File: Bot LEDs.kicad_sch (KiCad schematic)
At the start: 28 parts

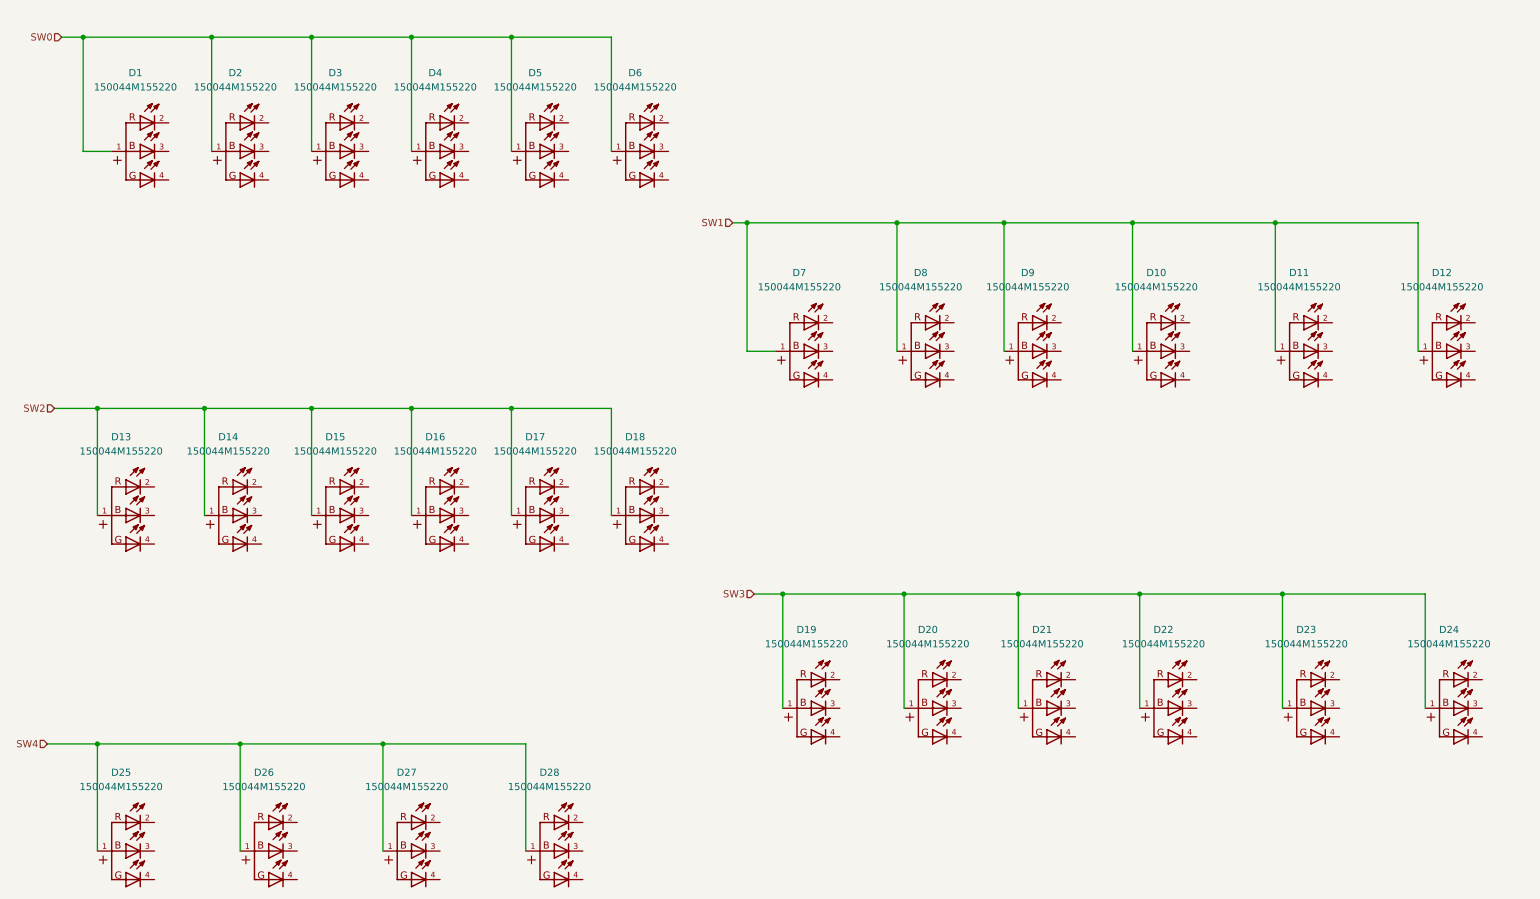
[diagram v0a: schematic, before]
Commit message: Initial complete implementation of LEDS.
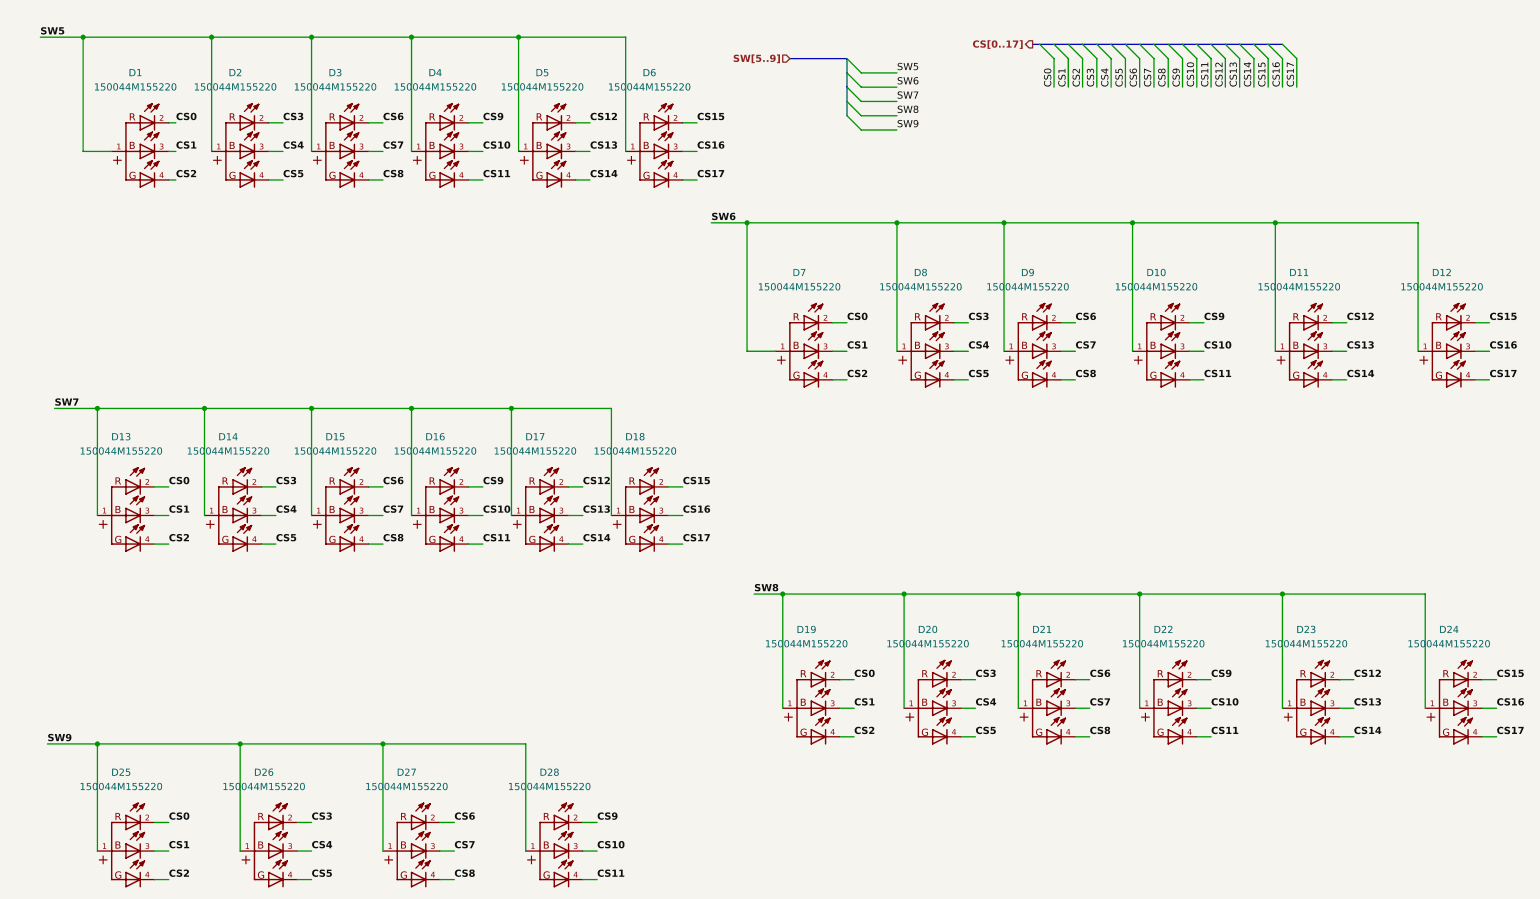
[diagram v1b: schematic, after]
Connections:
- net CS9: now reaches D28.2
- net CS9: now also D10.2, D16.2, D22.2, D4.2
- net CS10: now reaches D28.3
- net CS10: now also D10.3, D16.3, D22.3, D4.3
- net CS11: now reaches D28.4
- net CS11: now also D10.4, D16.4, D22.4, D4.4
- net CS12: now reaches D23.2
- net CS12: now also D11.2, D17.2, D5.2
- net CS13: now reaches D23.3
- net CS13: now also D11.3, D17.3, D5.3
- net CS14: now reaches D23.4
- net CS14: now also D11.4, D17.4, D5.4
- net CS3: now reaches D2.2
- net CS3: now also D14.2, D20.2, D26.2, D8.2
- net CS4: now reaches D2.3
- net CS4: now also D14.3, D20.3, D26.3, D8.3
- net CS5: now reaches D2.4
- net CS5: now also D14.4, D20.4, D26.4, D8.4
- net CS15: now reaches D6.2
- net CS15: now also D12.2, D18.2, D24.2
- net CS16: now reaches D6.3
- net CS16: now also D12.3, D18.3, D24.3
- net CS17: now reaches D6.4
- net CS17: now also D12.4, D18.4, D24.4
- net CS6: now reaches D3.2
- net CS6: now also D15.2, D21.2, D27.2, D9.2
- net CS7: now reaches D3.3
- net CS7: now also D15.3, D21.3, D27.3, D9.3
- net CS8: now reaches D3.4
- net CS8: now also D15.4, D21.4, D27.4, D9.4
- net CS0: now reaches D13.2
- net CS0: now also D1.2, D19.2, D25.2, D7.2
- net CS1: now reaches D13.3
- net CS1: now also D1.3, D19.3, D25.3, D7.3
- net CS2: now reaches D13.4
- net CS2: now also D1.4, D19.4, D25.4, D7.4
- net SW0 renamed SW5
- net SW1 renamed SW6
- net SW2 renamed SW7
- net SW3 renamed SW8
- net SW4 renamed SW9
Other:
- moved on the sheet: D5, D6

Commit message: First complete schematic with TPs.
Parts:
- added TP21, TP22, TP23, TP24, TP25: TestPoint, TestPoint:TestPoint_Pad_D1.0mm, symbol Connector:TestPoint
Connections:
- net SW5: now also TP21.1
- net SW6: now also TP22.1
- net SW7: now also TP23.1
- net SW8: now also TP24.1
- net SW9: now also TP25.1

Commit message: Added comments on schematic and fixed bus for SW[0..4] on Bot LEDs.
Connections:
- net SW5 renamed SW0
- net SW6 renamed SW1
- net SW7 renamed SW2
- net SW8 renamed SW3
- net SW9 renamed SW4
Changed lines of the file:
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@@
 		)
 	)
-	(label "SW6"
+	(label "SW1"
 		(at 168.91 26.67 0)
 		(effects
@@
 		)
 	)
-	(label "SW8"
+	(label "SW3"
 		(at 143.51 116.84 0)
 		(effects
@@
 		)
 	)
-	(label "SW9"
+	(label "SW4"
 		(at 168.91 34.29 0)
 		(effects
@@
 		)
 	)
-	(label "SW9"
+	(label "SW4"
 		(at 17.78 143.51 0)
 		(effects
@@
 		)
 	)
-	(label "SW8"
+	(label "SW3"
 		(at 168.91 31.75 0)
 		(effects
@@
 		)
 	)
-	(label "SW5"
+	(label "SW0"
 		(at 168.91 24.13 0)
 		(effects
@@
 		)
 	)
-	(label "SW7"
+	(label "SW2"
 		(at 19.05 83.82 0)
 		(effects
@@
 		)
 	)
-	(label "SW7"
+	(label "SW2"
 		(at 168.91 29.21 0)
 		(effects
@@
 		)
 	)
-	(label "SW5"
+	(label "SW0"
 		(at 16.51 17.78 0)
 		(effects
@@
 		)
 	)
-	(label "SW6"
+	(label "SW1"
 		(at 135.89 50.8 0)
 		(effects
@@
 		)
 	)
-	(hierarchical_label "SW[5..9]"
+	(hierarchical_label "SW[0..4]"
 		(shape input)
 		(at 149.86 21.59 180)

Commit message: Re-annotated entire schematic.
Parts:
- renumbered TP21 to TP24, TP22 to TP25, TP23 to TP26, TP24 to TP27, TP25 to TP28
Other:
- title: (none) -> Hourglass
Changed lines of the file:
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@@
 	(generator_version "9.0")
 	(paper "A4")
+	(title_block
+		(title "Hourglass")
+		(date "2025-04-23")
+		(rev "01")
+	)
 	(junction
 		(at 212.09 116.84)
@@
 		(dnp no)
 		(fields_autoplaced yes)
-		(property "Reference" "TP24"
+		(property "Reference" "TP27"
 			(at 151.13 113.5379 0)
 			(effects
@@
 			(project "Hourglass_PCBA"
 				(path "/a75630d2-15a7-42bc-8ce0-7846cbd1da6b/9c708963-e8cc-42a5-9c83-1e957695e1ca/1fa20d35-601e-473f-95b5-1a61e832d90c"
-					(reference "TP24")
+					(reference "TP27")
 					(unit 1)
 				)
@@
 		(dnp no)
 		(fields_autoplaced yes)
-		(property "Reference" "TP23"
+		(property "Reference" "TP26"
 			(at 29.21 80.5179 0)
 			(effects
@@
 			(project "Hourglass_PCBA"
 				(path "/a75630d2-15a7-42bc-8ce0-7846cbd1da6b/9c708963-e8cc-42a5-9c83-1e957695e1ca/1fa20d35-601e-473f-95b5-1a61e832d90c"
-					(reference "TP23")
+					(reference "TP26")
 					(unit 1)
 				)
@@
 		(dnp no)
 		(fields_autoplaced yes)
-		(property "Reference" "TP21"
+		(property "Reference" "TP24"
 			(at 26.67 14.4779 0)
 			(effects
@@
 			(project ""
 				(path "/a75630d2-15a7-42bc-8ce0-7846cbd1da6b/9c708963-e8cc-42a5-9c83-1e957695e1ca/1fa20d35-601e-473f-95b5-1a61e832d90c"
-					(reference "TP21")
+					(reference "TP24")
 					(unit 1)
 				)
@@
 		(dnp no)
 		(fields_autoplaced yes)
-		(property "Reference" "TP22"
+		(property "Reference" "TP25"
 			(at 144.78 47.4979 0)
 			(effects
@@
 			(project "Hourglass_PCBA"
 				(path "/a75630d2-15a7-42bc-8ce0-7846cbd1da6b/9c708963-e8cc-42a5-9c83-1e957695e1ca/1fa20d35-601e-473f-95b5-1a61e832d90c"
-					(reference "TP22")
+					(reference "TP25")
 					(unit 1)
 				)
@@
 		(dnp no)
 		(fields_autoplaced yes)
-		(property "Reference" "TP25"
+		(property "Reference" "TP28"
 			(at 29.21 140.2079 0)
 			(effects
@@
 			(project "Hourglass_PCBA"
 				(path "/a75630d2-15a7-42bc-8ce0-7846cbd1da6b/9c708963-e8cc-42a5-9c83-1e957695e1ca/1fa20d35-601e-473f-95b5-1a61e832d90c"
-					(reference "TP25")
+					(reference "TP28")
 					(unit 1)
 				)

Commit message: Started routing all of the SW sides.
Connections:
- net SW4: no longer D27.1, D28.1
- new net: D27.1, D28.1
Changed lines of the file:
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@@
-	)
-	(junction
-		(at 77.47 143.51)
-		(diameter 0)
-		(color 0 0 0 0)
 	)
 	(junction
@@
 	)
 	(junction
-		(at 52.07 143.51)
-		(diameter 0)
-		(color 0 0 0 0)
-	)
-	(junction
 		(at 82.55 17.78)
 		(diameter 0)
@@
 	(wire
 		(pts
-			(xy 102.87 143.51) (xy 77.47 143.51)
-		)
-		(stroke
-			(width 0)
-			(type default)
-		)
-	)
-	(wire
-		(pts
 			(xy 36.83 107.95) (xy 39.37 107.95)
 		)
@@
 	(wire
 		(pts
-			(xy 77.47 143.51) (xy 52.07 143.51)
-		)
-		(stroke
+			(xy 77.47 143.51) (xy 102.87 143.51)
+		)
+		(stroke

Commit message: Routed all of the SWx nets. Routing the CSx.
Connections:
- net SW4: now also D27.1, D28.1
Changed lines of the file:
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@@
+	)
+	(junction
+		(at 52.07 143.51)
+		(diameter 0)
+		(color 0 0 0 0)
 	)
 	(junction
@@
 	)
 	(junction
+		(at 77.47 143.51)
+		(diameter 0)
+		(color 0 0 0 0)
+	)
+	(junction
 		(at 148.59 116.84)
 		(diameter 0)
@@
 		)
 		(stroke
+			(width 0)
+			(type default)
+		)
+	)
+	(wire
+		(pts
+			(xy 52.07 143.51) (xy 77.47 143.51)
+		)
+		(stroke
